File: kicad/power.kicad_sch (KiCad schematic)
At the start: 53 parts, among them P1 VBAT, P2 GND, P3 10V, P4 GND, Q2 NX7002AK, U1 LMR38020FSDDAR, U2 LMR38020FSDDAR, U4 LP38692MP-3.3, U5 LP5907MFX-3.3

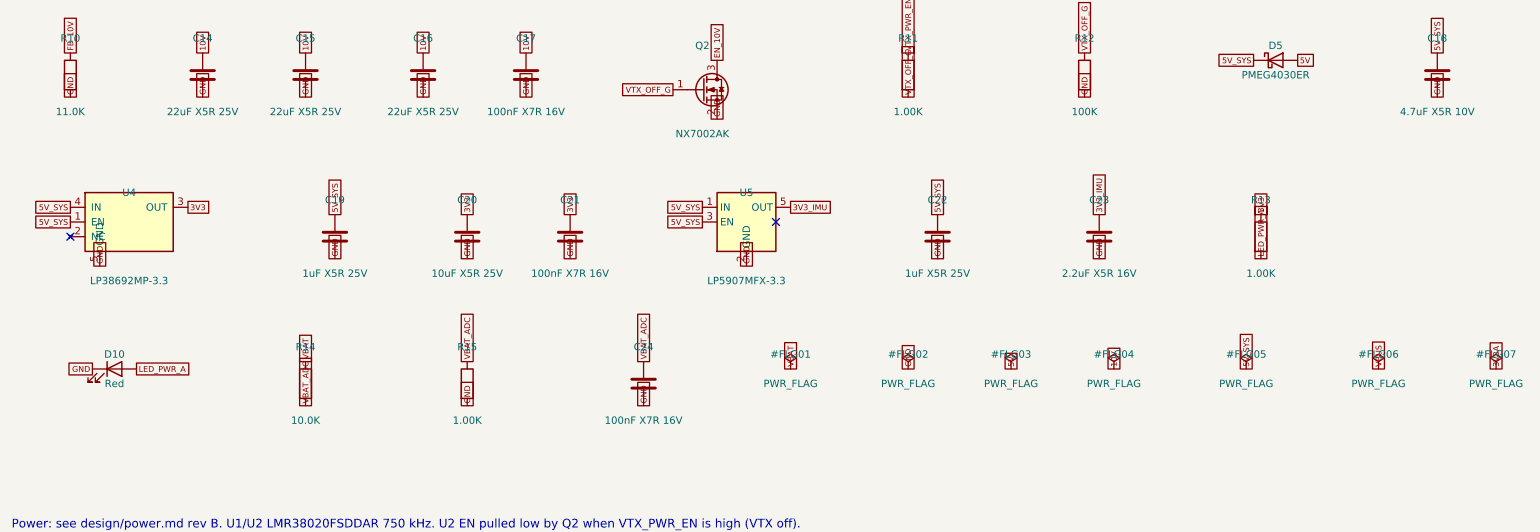
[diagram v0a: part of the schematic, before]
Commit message: Gate 1 fixes (crystal gm evidence, LDO output ESR, X7R caps, 50V HF cap, per-MPN datasheets, in_bom flags, project-file merge, parity fields), power re-audit fixes (board-level thermal envelope, USB inrush deviation, R41 VTX 0R link), PCB placement + legalizer + grommet keepouts; Gate 1 reports
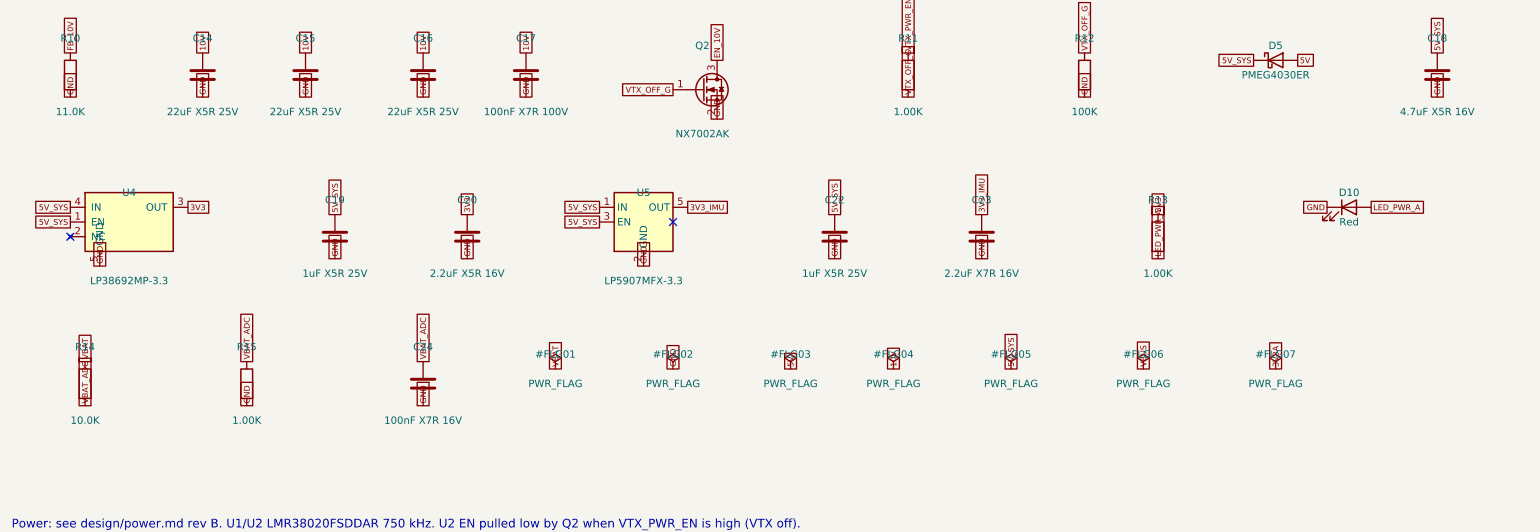
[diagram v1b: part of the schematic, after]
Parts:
- removed C21: 100nF X7R 16V, Capacitor_SMD:C_0402_1005Metric, symbol Device:C
- C17: value 100nF X7R 16V -> 100nF X7R 100V; footprint Capacitor_SMD:C_0402_1005Metric -> Capacitor_SMD:C_0603_1608Metric; DigiKey 1276-1001-1-ND -> 490-3285-1-ND (verify); MPN CL05B104KO5NNNC -> GRM188R72A104KA35D; Manufacturer Samsung Electro-Mechanics -> Murata
- C18: value 4.7uF X5R 10V -> 4.7uF X5R 16V
- C20: value 10uF X5R 25V -> 2.2uF X5R 16V; footprint Capacitor_SMD:C_0805_2012Metric -> Capacitor_SMD:C_0603_1608Metric; DigiKey 1276-2891-1-ND (verify) -> 1276-1183-1-ND (verify); MPN CL21A106KAYNNNE -> CL10A225KO8NNNC
- C23: value 2.2uF X5R 16V -> 2.2uF X7R 16V; DigiKey 1276-1183-1-ND (verify) -> 1276-1184-1-ND (verify); MPN CL10A225KO8NNNC -> CL10B225KO8NNNC
- P1, P2, P3, P4: now left out of the parts list
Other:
- moved on the sheet: C22, C23, C24, D10, R13, R14, R15, U5

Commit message: Gate 2 sourcing: apply DigiKey drop-in replacements (G2S-01/02/03/09), PN corrections, regenerate BOM; sourcing report and DigiKey BOM CSVs
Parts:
- C18: DigiKey 1276-1044-1-ND (verify) -> 1276-1784-1-ND
- C20: DigiKey 1276-1183-1-ND (verify) -> 1276-1040-1-ND
- C23: value 2.2uF X7R 16V -> 2.2uF X7R 10V; DigiKey 1276-1184-1-ND (verify) -> 1276-1134-1-ND; MPN CL10B225KO8NNNC -> CL10B225KP8NNNC
- L2: DigiKey 732-74438357082CT-ND (verify) -> 732-11205-1-ND
- Q2: MPN NX7002AKR -> NX7002AK,215
- R3, R8: DigiKey 311-34.8KLRCT-ND -> unconfirmed (BOM Manager matches by MPN); MPN RC0402FR-0734K8L -> ERJ-2RKF3482X; Manufacturer Yageo -> Panasonic
- R5: DigiKey 311-24.3KLRCT-ND -> unconfirmed (BOM Manager matches by MPN); MPN RC0402FR-0724K3L -> ERJ-2RKF2432X; Manufacturer Yageo -> Panasonic
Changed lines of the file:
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@@
 			)
 		)
-		(property "Datasheet" "https://www.yageo.com/upload/media/product/productsearch/datasheet/rchip/PYu-RC_Group_51_RoHS_L_12.pdf"
+		(property "Datasheet" "https://industrial.panasonic.com/cdbs/www-data/pdf/RDA0000/AOA0000C304.pdf"
 			(at 48.26 66.04 0)
 			(effects
@@
 			)
 		)
-		(property "MPN" "RC0402FR-0734K8L"
+		(property "MPN" "ERJ-2RKF3482X"
 			(at 48.26 66.04 0)
 			(effects
@@
 			)
 		)
-		(property "Manufacturer" "Yageo"
+		(property "Manufacturer" "Panasonic"
 			(at 48.26 66.04 0)
 			(effects
@@
 			)
 		)
-		(property "DigiKey" "311-34.8KLRCT-ND"
+		(property "DigiKey" "unconfirmed (BOM Manager matches by MPN)"
 			(at 48.26 66.04 0)
 			(effects
@@
 			)
 		)
-		(property "Datasheet" "https://www.yageo.com/upload/media/product/productsearch/datasheet/rchip/PYu-RC_Group_51_RoHS_L_12.pdf"
+		(property "Datasheet" "https://industrial.panasonic.com/cdbs/www-data/pdf/RDA0000/AOA0000C304.pdf"
 			(at 142.24 66.04 0)
 			(effects
@@
 			)
 		)
-		(property "MPN" "RC0402FR-0724K3L"
+		(property "MPN" "ERJ-2RKF2432X"
 			(at 142.24 66.04 0)
 			(effects
@@
 			)
 		)
-		(property "Manufacturer" "Yageo"
+		(property "Manufacturer" "Panasonic"
 			(at 142.24 66.04 0)
 			(effects
@@
 			)
 		)
-		(property "DigiKey" "311-24.3KLRCT-ND"
+		(property "DigiKey" "unconfirmed (BOM Manager matches by MPN)"
 			(at 142.24 66.04 0)
 			(effects
@@
 			)
 		)
-		(property "Datasheet" "https://www.yageo.com/upload/media/product/productsearch/datasheet/rchip/PYu-RC_Group_51_RoHS_L_12.pdf"
+		(property "Datasheet" "https://industrial.panasonic.com/cdbs/www-data/pdf/RDA0000/AOA0000C304.pdf"
 			(at 193.04 88.9 0)
 			(effects
@@
 			)
 		)
-		(property "MPN" "RC0402FR-0734K8L"
+		(property "MPN" "ERJ-2RKF3482X"
 			(at 193.04 88.9 0)
 			(effects
@@
 			)
 		)
-		(property "Manufacturer" "Yageo"
+		(property "Manufacturer" "Panasonic"
 			(at 193.04 88.9 0)
 			(effects
@@
 			)
 		)
-		(property "DigiKey" "311-34.8KLRCT-ND"
+		(property "DigiKey" "unconfirmed (BOM Manager matches by MPN)"
 			(at 193.04 88.9 0)
 			(effects
@@
 			)
 		)
-		(property "DigiKey" "732-74438357082CT-ND (verify)"
+		(property "DigiKey" "732-11205-1-ND"
 			(at 246.38 88.9 0)
 			(effects
@@
 			)
 		)
-		(property "MPN" "NX7002AKR"
+		(property "MPN" "NX7002AK,215"
 			(at 134.62 121.92 0)
 			(effects
@@
 			)
 		)
-		(property "DigiKey" "1276-1044-1-ND (verify)"
+		(property "DigiKey" "1276-1784-1-ND"
 			(at 261.62 119.38 0)
 			(effects
@@
 			)
 		)
-		(property "DigiKey" "1276-1183-1-ND (verify)"
+		(property "DigiKey" "1276-1040-1-ND"
 			(at 93.98 147.32 0)
 			(effects
@@
 			)
 		)
-		(property "Value" "2.2uF X7R 16V"
+		(property "Value" "2.2uF X7R 10V"
 			(at 182.88 153.67 0)
 			(effects
@@
 			)
 		)
-		(property "Datasheet" "https://product.samsungsem.com/mlcc/CL10B225KO8NNNC.do"
+		(property "Datasheet" "https://product.samsungsem.com/mlcc/CL10B225KP8NNNC.do"
 			(at 182.88 147.32 0)
 			(effects
@@
 			)
 		)
-		(property "MPN" "CL10B225KO8NNNC"
+		(property "MPN" "CL10B225KP8NNNC"
 			(at 182.88 147.32 0)
 			(effects
@@
 			)
 		)
-		(property "DigiKey" "1276-1184-1-ND (verify)"
+		(property "DigiKey" "1276-1134-1-ND"
 			(at 182.88 147.32 0)
 			(effects

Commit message: WIP Gate 3 rework: pin-anchored placement, tight legalizer, placecheck; WE-MAPI 4020 inductors, GRM32DR input caps
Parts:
- C1, C10, C11, C2, C3: value 10uF X7R 50V -> 10uF X7R 50V 2.0mm; DigiKey 1276-3387-1-ND -> 490-GRM32DR71H106KA01LCT-ND (verify); MPN CL32B106KBJNNNE -> GRM32DR71H106KA01L; Manufacturer Samsung Electro-Mechanics -> Murata
- L1: value 6.8uH -> 5.6uH; footprint Inductor_SMD:L_Wuerth_MAPI-4030 -> Inductor_SMD:L_Wuerth_MAPI-4020; DigiKey 732-11204-1-ND -> unconfirmed (BOM Manager matches by MPN); MPN 74438357068 -> 74438356056
- L2: value 8.2uH -> 5.6uH; footprint Inductor_SMD:L_Wuerth_MAPI-4030 -> Inductor_SMD:L_Wuerth_MAPI-4020; DigiKey 732-11205-1-ND -> unconfirmed (BOM Manager matches by MPN); MPN 74438357082 -> 74438356056
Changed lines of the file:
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@@
 			)
 		)
-		(property "Value" "10uF X7R 50V"
+		(property "Value" "10uF X7R 50V 2.0mm"
 			(at 129.54 41.91 0)
 			(effects
@@
 			)
 		)
-		(property "Datasheet" "https://product.samsungsem.com/mlcc/CL32B106KBJNNNE.do"
+		(property "Datasheet" "https://search.murata.co.jp/Ceramy/image/img/A01X/G101/ENG/GRM32DR71H106KA01-01.pdf"
 			(at 129.54 35.56 0)
 			(effects
@@
 			)
 		)
-		(property "MPN" "CL32B106KBJNNNE"
+		(property "MPN" "GRM32DR71H106KA01L"
 			(at 129.54 35.56 0)
 			(effects
@@
 			)
 		)
-		(property "Manufacturer" "Samsung Electro-Mechanics"
+		(property "Manufacturer" "Murata"
 			(at 129.54 35.56 0)
 			(effects
@@
 			)
 		)
-		(property "DigiKey" "1276-3387-1-ND"
+		(property "DigiKey" "490-GRM32DR71H106KA01LCT-ND (verify)"
 			(at 129.54 35.56 0)
 			(effects
@@
 			)
 		)
-		(property "Value" "10uF X7R 50V"
+		(property "Value" "10uF X7R 50V 2.0mm"
 			(at 203.2 41.91 0)
 			(effects
@@
 			)
 		)
-		(property "Datasheet" "https://product.samsungsem.com/mlcc/CL32B106KBJNNNE.do"
+		(property "Datasheet" "https://search.murata.co.jp/Ceramy/image/img/A01X/G101/ENG/GRM32DR71H106KA01-01.pdf"
 			(at 203.2 35.56 0)
 			(effects
@@
 			)
 		)
-		(property "MPN" "CL32B106KBJNNNE"
+		(property "MPN" "GRM32DR71H106KA01L"
 			(at 203.2 35.56 0)
 			(effects
@@
 			)
 		)
-		(property "Manufacturer" "Samsung Electro-Mechanics"
+		(property "Manufacturer" "Murata"
 			(at 203.2 35.56 0)
 			(effects
@@
 			)
 		)
-		(property "DigiKey" "1276-3387-1-ND"
+		(property "DigiKey" "490-GRM32DR71H106KA01LCT-ND (verify)"
 			(at 203.2 35.56 0)
 			(effects
@@
 			)
 		)
-		(property "Value" "10uF X7R 50V"
+		(property "Value" "10uF X7R 50V 2.0mm"
 			(at 226.06 41.91 0)
 			(effects
@@
 			)
 		)
-		(property "Datasheet" "https://product.samsungsem.com/mlcc/CL32B106KBJNNNE.do"
+		(property "Datasheet" "https://search.murata.co.jp/Ceramy/image/img/A01X/G101/ENG/GRM32DR71H106KA01-01.pdf"
 			(at 226.06 35.56 0)
 			(effects
@@
 			)
 		)
-		(property "MPN" "CL32B106KBJNNNE"
+		(property "MPN" "GRM32DR71H106KA01L"
 			(at 226.06 35.56 0)
 			(effects
@@
 			)
 		)
-		(property "Manufacturer" "Samsung Electro-Mechanics"
+		(property "Manufacturer" "Murata"
 			(at 226.06 35.56 0)
 			(effects
@@
 			)
 		)
-		(property "DigiKey" "1276-3387-1-ND"
+		(property "DigiKey" "490-GRM32DR71H106KA01LCT-ND (verify)"
 			(at 226.06 35.56 0)
 			(effects
@@
 			)
 		)
-		(property "Value" "6.8uH"
+		(property "Value" "5.6uH"
 			(at 96.52 72.39 0)
 			(effects
@@
 			)
 		)
-		(property "Footprint" "Inductor_SMD:L_Wuerth_MAPI-4030"
+		(property "Footprint" "Inductor_SMD:L_Wuerth_MAPI-4020"
 			(at 96.52 66.04 0)
 			(effects
@@
 			)
 		)
-		(property "Datasheet" "https://www.we-online.com/components/products/datasheet/74438357068.pdf"
+		(property "Datasheet" "https://www.we-online.com/components/products/datasheet/74438356056.pdf"
 			(at 96.52 66.04 0)
 			(effects
@@
 			)
 		)
-		(property "Description" "WE-MAPI 4030 power inductor"
+		(property "Description" "WE-MAPI 4020 power inductor"
 			(at 96.52 66.04 0)
 			(effects
@@
 			)
 		)
-		(property "MPN" "74438357068"
+		(property "MPN" "74438356056"
 			(at 96.52 66.04 0)
 			(effects
@@
 			)
 		)
-		(property "DigiKey" "732-11204-1-ND"
+		(property "DigiKey" "unconfirmed (BOM Manager matches by MPN)"
 			(at 96.52 66.04 0)
 			(effects
@@
 			)
 		)
-		(property "Value" "10uF X7R 50V"
+		(property "Value" "10uF X7R 50V 2.0mm"
 			(at 78.74 95.25 0)
 			(effects
@@
 			)
 		)
-		(property "Datasheet" "https://product.samsungsem.com/mlcc/CL32B106KBJNNNE.do"
+		(property "Datasheet" "https://search.murata.co.jp/Ceramy/image/img/A01X/G101/ENG/GRM32DR71H106KA01-01.pdf"
 			(at 78.74 88.9 0)
 			(effects
@@
 			)
 		)
-		(property "MPN" "CL32B106KBJNNNE"
+		(property "MPN" "GRM32DR71H106KA01L"
 			(at 78.74 88.9 0)
 			(effects
@@
 			)
 		)
-		(property "Manufacturer" "Samsung Electro-Mechanics"
+		(property "Manufacturer" "Murata"
 			(at 78.74 88.9 0)
 			(effects
@@
 			)
 		)
-		(property "DigiKey" "1276-3387-1-ND"
+		(property "DigiKey" "490-GRM32DR71H106KA01LCT-ND (verify)"
 			(at 78.74 88.9 0)
 			(effects
@@
 			)
 		)
-		(property "Value" "10uF X7R 50V"
+		(property "Value" "10uF X7R 50V 2.0mm"
 			(at 99.06 95.25 0)
 			(effects
@@
 			)
 		)
-		(property "Datasheet" "https://product.samsungsem.com/mlcc/CL32B106KBJNNNE.do"
+		(property "Datasheet" "https://search.murata.co.jp/Ceramy/image/img/A01X/G101/ENG/GRM32DR71H106KA01-01.pdf"
 			(at 99.06 88.9 0)
 			(effects
@@
 			)
 		)
-		(property "MPN" "CL32B106KBJNNNE"
+		(property "MPN" "GRM32DR71H106KA01L"
 			(at 99.06 88.9 0)
 			(effects
@@
 			)
 		)
-		(property "Manufacturer" "Samsung Electro-Mechanics"
+		(property "Manufacturer" "Murata"
 			(at 99.06 88.9 0)
 			(effects
@@
 			)
 		)
-		(property "DigiKey" "1276-3387-1-ND"
+		(property "DigiKey" "490-GRM32DR71H106KA01LCT-ND (verify)"
 			(at 99.06 88.9 0)
 			(effects
@@
 			)
 		)
-		(property "Value" "8.2uH"
+		(property "Value" "5.6uH"
 			(at 246.38 95.25 0)
 			(effects
@@
 			)
 		)
-		(property "Footprint" "Inductor_SMD:L_Wuerth_MAPI-4030"
+		(property "Footprint" "Inductor_SMD:L_Wuerth_MAPI-4020"
 			(at 246.38 88.9 0)
 			(effects
@@
 			)
 		)
-		(property "Datasheet" "https://www.we-online.com/components/products/datasheet/74438357082.pdf"
+		(property "Datasheet" "https://www.we-online.com/components/products/datasheet/74438356056.pdf"
 			(at 246.38 88.9 0)
 			(effects
@@
 			)
 		)
-		(property "Description" "WE-MAPI 4030 power inductor"
+		(property "Description" "WE-MAPI 4020 power inductor"
 			(at 246.38 88.9 0)
 			(effects
@@
 			)
 		)
-		(property "MPN" "74438357082"
+		(property "MPN" "74438356056"
 			(at 246.38 88.9 0)
 			(effects
@@
 			)
 		)
-		(property "DigiKey" "732-11205-1-ND"
+		(property "DigiKey" "unconfirmed (BOM Manager matches by MPN)"
 			(at 246.38 88.9 0)
 			(effects

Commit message: Gate 2 re-check: report + fixes (TDK 4.7uF 100V bottom input caps, PNs, BOM regenerated $175.73, inductor keepouts), D-20
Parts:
- C1: value 10uF X7R 50V 2.0mm -> 10uF X7R 50V; DigiKey 490-GRM32DR71H106KA01LCT-ND (verify) -> 1276-3387-1-ND; MPN GRM32DR71H106KA01L -> CL32B106KBJNNNE; Manufacturer Murata -> Samsung Electro-Mechanics
- C10, C11, C2, C3: value 10uF X7R 50V 2.0mm -> 4.7uF X7S 100V 2.0mm; DigiKey 490-GRM32DR71H106KA01LCT-ND (verify) -> 445-6042-1-ND (verify: K200AB cut tape); MPN GRM32DR71H106KA01L -> C3225X7S2A475K200AB; Manufacturer Murata -> TDK
- L1, L2: DigiKey unconfirmed (BOM Manager matches by MPN) -> not confirmed; alt 78438356056 = 732-11317-1-ND
- R3, R8: DigiKey unconfirmed (BOM Manager matches by MPN) -> P34.8KLCT-ND
- R5: DigiKey unconfirmed (BOM Manager matches by MPN) -> P24.3KLCT-ND
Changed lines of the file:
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@@
 			)
 		)
-		(property "Value" "10uF X7R 50V 2.0mm"
+		(property "Value" "10uF X7R 50V"
 			(at 129.54 41.91 0)
 			(effects
@@
 			)
 		)
-		(property "Datasheet" "https://search.murata.co.jp/Ceramy/image/img/A01X/G101/ENG/GRM32DR71H106KA01-01.pdf"
+		(property "Datasheet" "https://product.samsungsem.com/mlcc/CL32B106KBJNNNE.do"
 			(at 129.54 35.56 0)
 			(effects
@@
 			)
 		)
-		(property "MPN" "GRM32DR71H106KA01L"
+		(property "MPN" "CL32B106KBJNNNE"
 			(at 129.54 35.56 0)
 			(effects
@@
 			)
 		)
-		(property "Manufacturer" "Murata"
+		(property "Manufacturer" "Samsung Electro-Mechanics"
 			(at 129.54 35.56 0)
 			(effects
@@
 			)
 		)
-		(property "DigiKey" "490-GRM32DR71H106KA01LCT-ND (verify)"
+		(property "DigiKey" "1276-3387-1-ND"
 			(at 129.54 35.56 0)
 			(effects
@@
 			)
 		)
-		(property "Value" "10uF X7R 50V 2.0mm"
+		(property "Value" "4.7uF X7S 100V 2.0mm"
 			(at 203.2 41.91 0)
 			(effects
@@
 			)
 		)
-		(property "Datasheet" "https://search.murata.co.jp/Ceramy/image/img/A01X/G101/ENG/GRM32DR71H106KA01-01.pdf"
+		(property "Datasheet" "https://product.tdk.com/system/files/dam/doc/product/capacitor/ceramic/mlcc/catalog/mlcc_commercial_midvoltage_en.pdf"
 			(at 203.2 35.56 0)
 			(effects
@@
 			)
 		)
-		(property "MPN" "GRM32DR71H106KA01L"
+		(property "MPN" "C3225X7S2A475K200AB"
 			(at 203.2 35.56 0)
 			(effects
@@
 			)
 		)
-		(property "Manufacturer" "Murata"
+		(property "Manufacturer" "TDK"
 			(at 203.2 35.56 0)
 			(effects
@@
 			)
 		)
-		(property "DigiKey" "490-GRM32DR71H106KA01LCT-ND (verify)"
+		(property "DigiKey" "445-6042-1-ND (verify: K200AB cut tape)"
 			(at 203.2 35.56 0)
 			(effects
@@
 			)
 		)
-		(property "Value" "10uF X7R 50V 2.0mm"
+		(property "Value" "4.7uF X7S 100V 2.0mm"
 			(at 226.06 41.91 0)
 			(effects
@@
 			)
 		)
-		(property "Datasheet" "https://search.murata.co.jp/Ceramy/image/img/A01X/G101/ENG/GRM32DR71H106KA01-01.pdf"
+		(property "Datasheet" "https://product.tdk.com/system/files/dam/doc/product/capacitor/ceramic/mlcc/catalog/mlcc_commercial_midvoltage_en.pdf"
 			(at 226.06 35.56 0)
 			(effects
@@
 			)
 		)
-		(property "MPN" "GRM32DR71H106KA01L"
+		(property "MPN" "C3225X7S2A475K200AB"
 			(at 226.06 35.56 0)
 			(effects
@@
 			)
 		)
-		(property "Manufacturer" "Murata"
+		(property "Manufacturer" "TDK"
 			(at 226.06 35.56 0)
 			(effects
@@
 			)
 		)
-		(property "DigiKey" "490-GRM32DR71H106KA01LCT-ND (verify)"
+		(property "DigiKey" "445-6042-1-ND (verify: K200AB cut tape)"
 			(at 226.06 35.56 0)
 			(effects
@@
 			)
 		)
-		(property "DigiKey" "unconfirmed (BOM Manager matches by MPN)"
+		(property "DigiKey" "P34.8KLCT-ND"
 			(at 48.26 66.04 0)
 			(effects
@@
 			)
 		)
-		(property "DigiKey" "unconfirmed (BOM Manager matches by MPN)"
+		(property "DigiKey" "not confirmed; alt 78438356056 = 732-11317-1-ND"
 			(at 96.52 66.04 0)
 			(effects
@@
 			)
 		)
-		(property "DigiKey" "unconfirmed (BOM Manager matches by MPN)"
+		(property "DigiKey" "P24.3KLCT-ND"
 			(at 142.24 66.04 0)
 			(effects
@@
 			)
 		)
-		(property "Value" "10uF X7R 50V 2.0mm"
+		(property "Value" "4.7uF X7S 100V 2.0mm"
 			(at 78.74 95.25 0)
 			(effects
@@
 			)
 		)
-		(property "Datasheet" "https://search.murata.co.jp/Ceramy/image/img/A01X/G101/ENG/GRM32DR71H106KA01-01.pdf"
+		(property "Datasheet" "https://product.tdk.com/system/files/dam/doc/product/capacitor/ceramic/mlcc/catalog/mlcc_commercial_midvoltage_en.pdf"
 			(at 78.74 88.9 0)
 			(effects
@@
 			)
 		)
-		(property "MPN" "GRM32DR71H106KA01L"
+		(property "MPN" "C3225X7S2A475K200AB"
 			(at 78.74 88.9 0)
 			(effects
@@
 			)
 		)
-		(property "Manufacturer" "Murata"
+		(property "Manufacturer" "TDK"
 			(at 78.74 88.9 0)
 			(effects
@@
 			)
 		)
-		(property "DigiKey" "490-GRM32DR71H106KA01LCT-ND (verify)"
+		(property "DigiKey" "445-6042-1-ND (verify: K200AB cut tape)"
 			(at 78.74 88.9 0)
 			(effects
@@
 			)
 		)
-		(property "Value" "10uF X7R 50V 2.0mm"
+		(property "Value" "4.7uF X7S 100V 2.0mm"
 			(at 99.06 95.25 0)
 			(effects
@@
 			)
 		)
-		(property "Datasheet" "https://search.murata.co.jp/Ceramy/image/img/A01X/G101/ENG/GRM32DR71H106KA01-01.pdf"
+		(property "Datasheet" "https://product.tdk.com/system/files/dam/doc/product/capacitor/ceramic/mlcc/catalog/mlcc_commercial_midvoltage_en.pdf"
 			(at 99.06 88.9 0)
 			(effects
@@
 			)
 		)
-		(property "MPN" "GRM32DR71H106KA01L"
+		(property "MPN" "C3225X7S2A475K200AB"
 			(at 99.06 88.9 0)
 			(effects
@@
 			)
 		)
-		(property "Manufacturer" "Murata"
+		(property "Manufacturer" "TDK"
 			(at 99.06 88.9 0)
 			(effects
@@
 			)
 		)
-		(property "DigiKey" "490-GRM32DR71H106KA01LCT-ND (verify)"
+		(property "DigiKey" "445-6042-1-ND (verify: K200AB cut tape)"
 			(at 99.06 88.9 0)
 			(effects
@@
 			)
 		)
-		(property "DigiKey" "unconfirmed (BOM Manager matches by MPN)"
+		(property "DigiKey" "P34.8KLCT-ND"
 			(at 193.04 88.9 0)
 			(effects
@@
 			)
 		)
-		(property "DigiKey" "unconfirmed (BOM Manager matches by MPN)"
+		(property "DigiKey" "not confirmed; alt 78438356056 = 732-11317-1-ND"
 			(at 246.38 88.9 0)
 			(effects
